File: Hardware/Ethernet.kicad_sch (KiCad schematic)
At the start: 31 parts, among them J5 MagJack_PoE, U4 KSZ8041NL/I

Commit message: PCB symbol updates
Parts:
- removed C9: 1nF, SparkFun-Capacitor:C_1206_3216Metric, symbol SparkFun-Capacitor:1.0nF_1206V_2kV_10%
- added C9: 1nF, SparkFun-Capacitor:C_1206_3216Metric, symbol SparkFun-Capacitor:1.0nF_1206_2kV_10%
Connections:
- net GND: now also C9.2
- net GND-ISO: now also C9.1

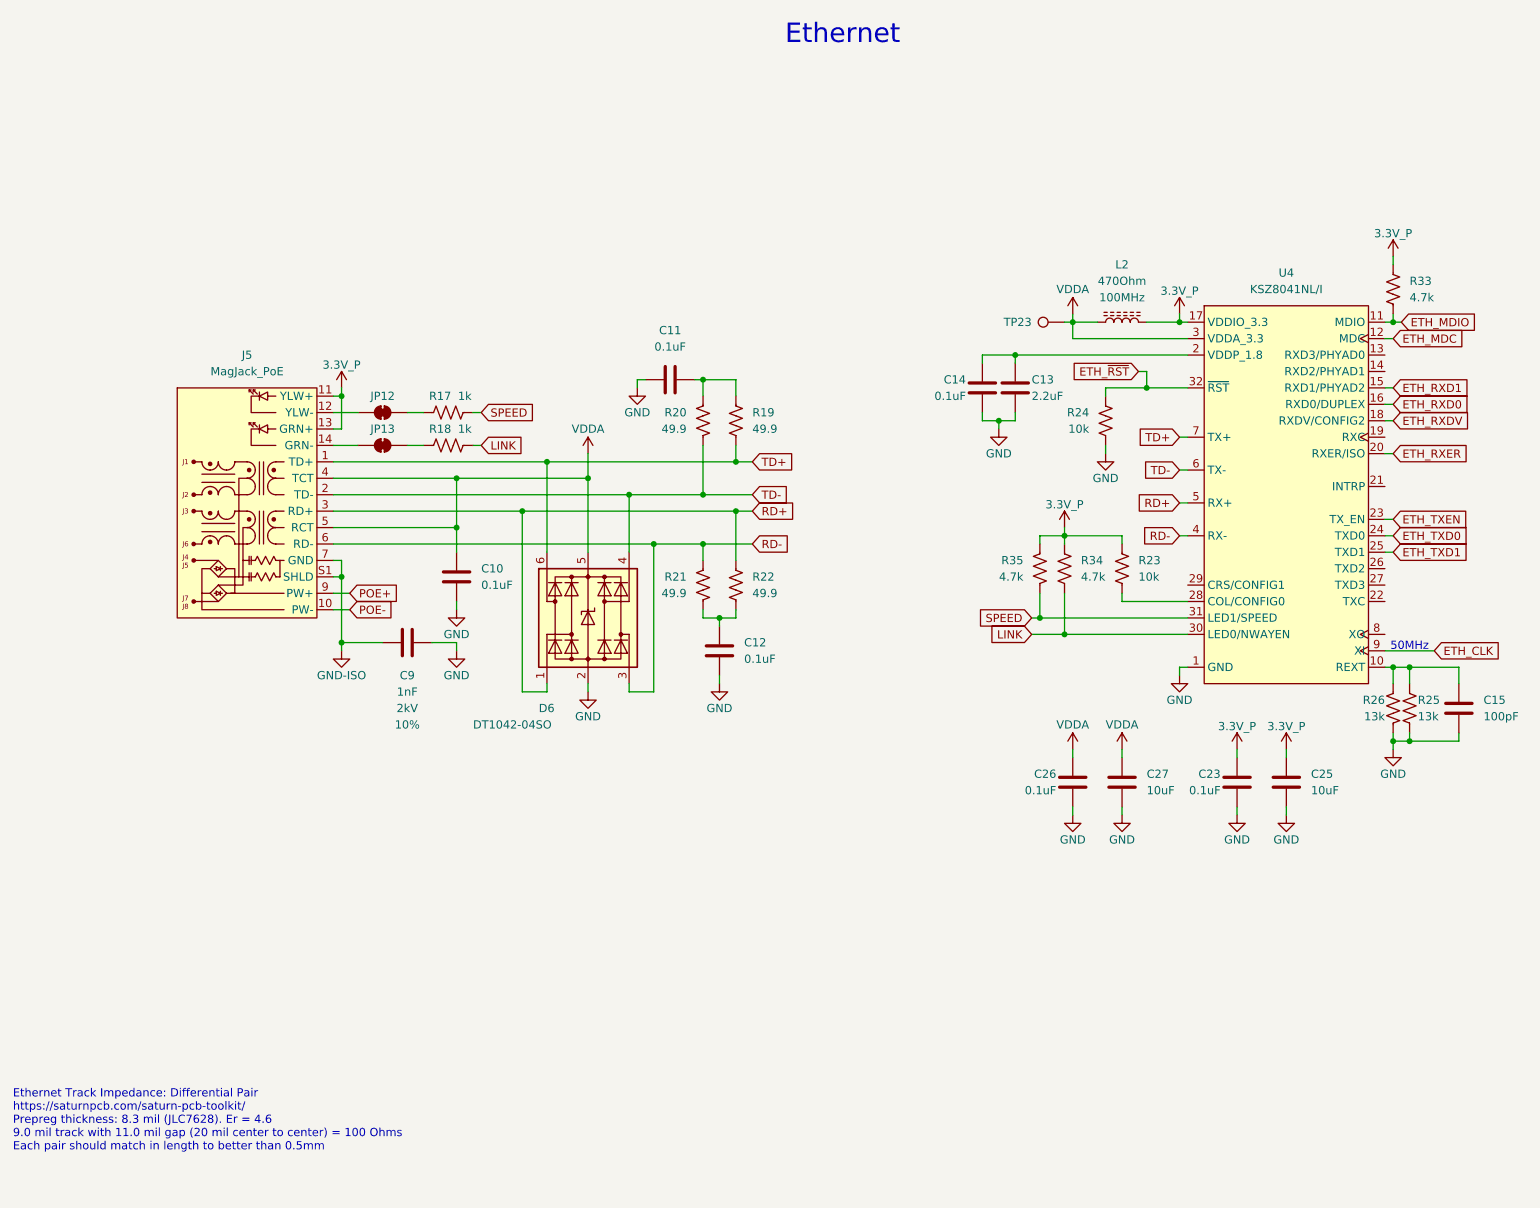
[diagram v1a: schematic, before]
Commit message: Updates for v1.0 PCB
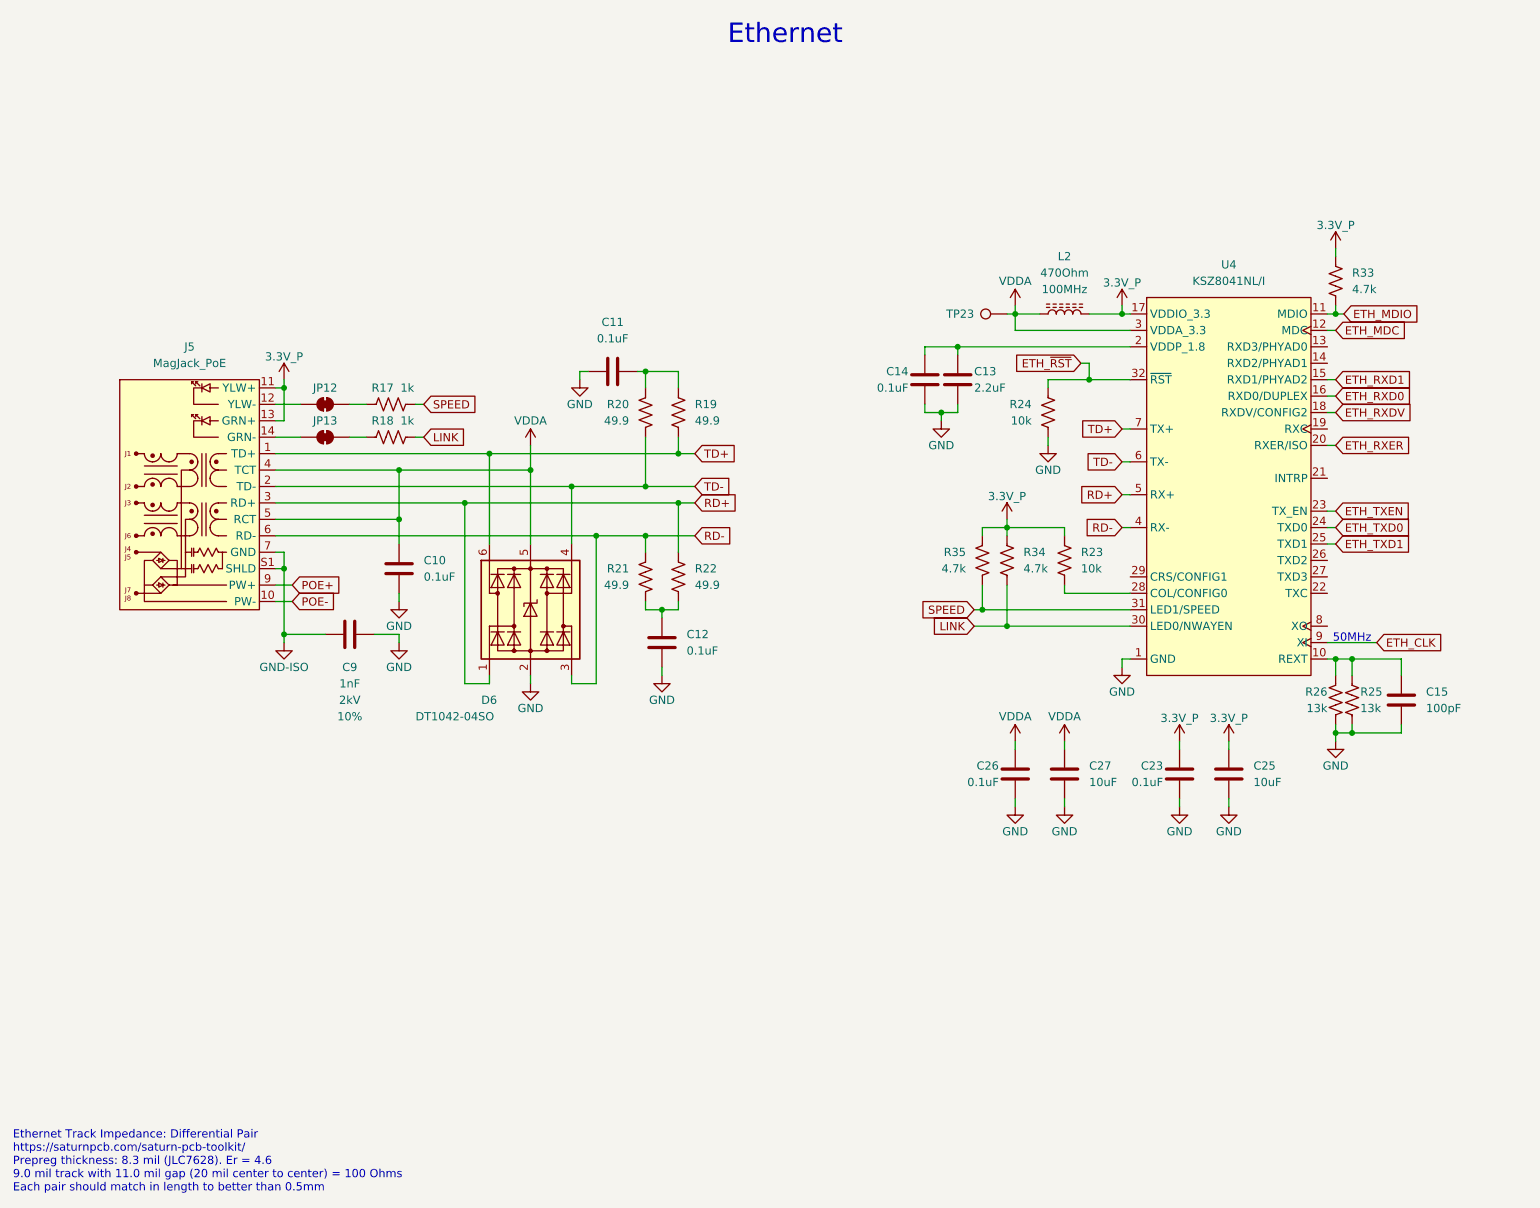
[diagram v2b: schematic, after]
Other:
- title: (none) -> Ethernet
- moved on the sheet: C10, C11, C12, C13, C14, C15, C23, C25, C26, C27, C9, D6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
